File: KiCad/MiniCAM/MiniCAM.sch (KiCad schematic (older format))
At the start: 66 parts, among them J1 SMA-J-P-H-RA-TH1, J2 Conn_01x02, J3 Conn_01x03, J4 Conn_02x03_Odd_Even, U1 NCV8154MW180280TBG, U2 DS90UB933-Q1, U3 MT9P031, U4 SiT_2.5mmx2mm

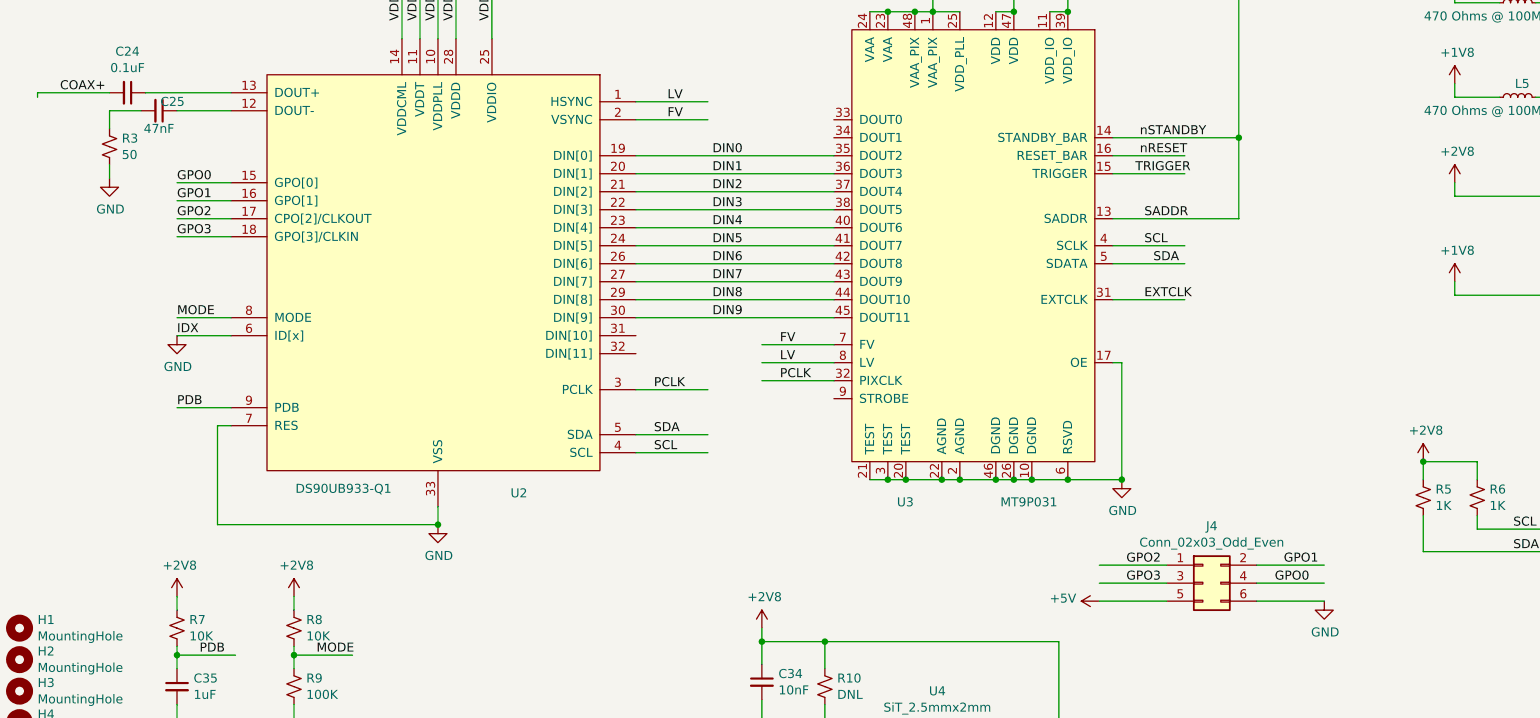
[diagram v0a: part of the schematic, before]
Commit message: Add connection to TRIG pin of sensor along with 0 resistors
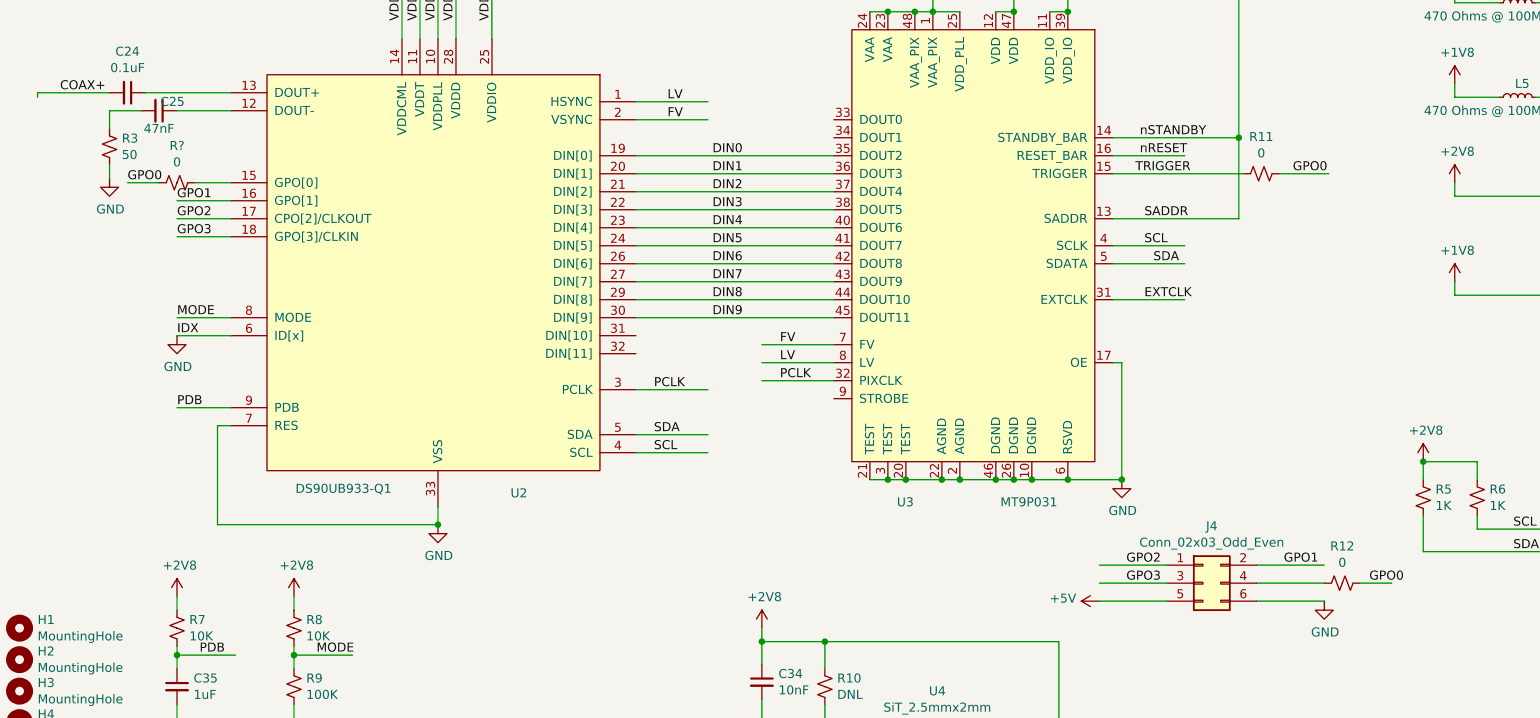
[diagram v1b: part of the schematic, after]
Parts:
- added R11, R12, R?: 0, .Resistor:R_0402_1005Metric_ERJ_L, symbol .Device:R_Small_US
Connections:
- wire segments 221 -> 224
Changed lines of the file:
@@
 $EndComp
 Wire Wire Line
-	1900 3925 1600 3925
+	1900 3925 1700 3925
 Wire Wire Line
 	1900 4025 1600 4025
@@
 Wire Wire Line
 	1900 4225 1600 4225
-Text Label 1600 3925 0    50   ~ 0
+Text Label 1325 3925 0    50   ~ 0
 GPO0
 Text Label 1600 4025 0    50   ~ 0
@@
 Wire Wire Line
 	6800 4275 7200 4275
-Wire Wire Line
-	6800 3875 7200 3875
 Wire Wire Line
 	6800 3775 7200 3775
@@
 Wire Wire Line
 	7975 6250 7600 6250
-Text Label 7700 6150 0    50   ~ 0
+Text Label 8225 6150 0    50   ~ 0
 GPO0
 Text Label 7750 6050 0    50   ~ 0
@@
 	11100 825  10775 825
 Connection ~ 10775 825
+Text Label 7800 3875 0    50   ~ 0
+GPO0
+$Comp
+L .Device:R_Small_US R11
+U 1 1 5F170FBC
+P 7625 3875
+F 0 "R11" V 7420 3875 50  0000 C CNN
+F 1 "0" V 7511 3875 50  0000 C CNN
+F 2 ".Resistor:R_0402_1005Metric_ERJ_L" H 7625 3875 50  0001 C CNN
+F 3 "~" H 7625 3875 50  0001 C CNN
+	1    7625 3875
+	0    1    1    0
+$EndComp
+Wire Wire Line
+	6800 3875 7525 3875
+Wire Wire Line
+	7725 3875 8000 3875
+$Comp
+L .Device:R_Small_US R12
+U 1 1 5F1A0E57
+P 8075 6150
+F 0 "R12" V 7870 6150 50  0000 C CNN
+F 1 "0" V 7961 6150 50  0000 C CNN
+F 2 ".Resistor:R_0402_1005Metric_ERJ_L" H 8075 6150 50  0001 C CNN
+F 3 "~" H 8075 6150 50  0001 C CNN
+	1    8075 6150
+	0    1    1    0
+$EndComp
+Wire Wire Line
+	8175 6150 8350 6150
+$Comp
+L .Device:R_Small_US R?
+U 1 1 5F1C723A
+P 1600 3925
+F 0 "R?" V 1395 3925 50  0000 C CNN
+F 1 "0" V 1486 3925 50  0000 C CNN
+F 2 ".Resistor:R_0402_1005Metric_ERJ_L" H 1600 3925 50  0001 C CNN
+F 3 "~" H 1600 3925 50  0001 C CNN
+	1    1600 3925
+	0    1    1    0
+$EndComp
+Wire Wire Line
+	1325 3925 1500 3925
 $EndSCHEMATC

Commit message: Forgot to save schematic for last commit. Here it is.
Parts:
- gave numbers to parts that had none: 1
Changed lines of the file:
@@
 	8175 6150 8350 6150
 $Comp
-L .Device:R_Small_US R?
+L .Device:R_Small_US R13
 U 1 1 5F1C723A
 P 1600 3925
-F 0 "R?" V 1395 3925 50  0000 C CNN
+F 0 "R13" V 1395 3925 50  0000 C CNN
 F 1 "0" V 1486 3925 50  0000 C CNN
 F 2 ".Resistor:R_0402_1005Metric_ERJ_L" H 1600 3925 50  0001 C CNN

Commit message: Generate BOM, PnP, Gerbers. Check and correct DRC errors. v0.1
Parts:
- C1, C11, C16, C2, C3, C33, C35: Part Number (none) -> GRT155R61C105KE01D
- C10, C14, C15, C19, C22, C24, C27, C30, C32, C4, C5, C6, C7, C8, C9: Part Number (none) -> GCM155R71C104KA55J
- C12, C13, C17, C36: Part Number (none) -> GRM188R61A106KE69J
- C18, C21, C26, C29, C31, C34: Part Number (none) -> GCM155R71E103KA37D
- C20, C23, C28: Part Number (none) -> CC0402MRX5R6BB475
- C25: Part Number (none) -> GRM155R71A473KA01D
- D1: Part Number (none) -> LTST-C190KRKT
- H1, H2, H3, H4, H5, H6, J2, J3, J4, R10, U3, U4: Part Number (none) -> DNL
- J1: Part Number (none) -> CONSMA001-SMD-G-T
- L1, L3, L4, L5: Part Number (none) -> BLM18PG471SN1D
- L2: Part Number (none) -> ADL3225V-470MT-TL000
- R1: Part Number (none) -> ERJ-2RKF2001X
- R11, R12, R13: Part Number (none) -> ERJ-2GE0R00X
- R2: Part Number (none) -> ERJ-2RKF4990X
- R3: Part Number (none) -> ERJ-2RKF49R9X
- R4: Part Number (none) -> ERJ-2GEJ102X
- R5, R6: value 1K -> 2K; Part Number (none) -> ERJ-2RKF2001X
- R7, R8: Part Number (none) -> ERJ-2RKF1002X
- R9: Part Number (none) -> ERJ-2RKF1003X
- U1: Part Number (none) -> NCV8154MW180280TBG
- U2: Part Number (none) -> DS90UB913ATRTVTQ1
